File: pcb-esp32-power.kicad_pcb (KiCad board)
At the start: 2 copper layers, 52.6 x 47.4 mm, 41 parts, among them IC1 TP4054-42-SOT25-R, IC2 SY8008B, J1 C-OBD-II-16M, J2 Bus_Connector, J3 Conn_01x02, Q1 Si2307BDS, U1 STEPDOWN12_5, U2 LTC3530EMS

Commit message: OBD Pin 4 & 5 an Masse
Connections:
- J1 pad 4: Net-(J1-Pad4) -> GND

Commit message: Erste Version mit LTC4091
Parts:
- removed C2: 100nF, Capacitor_SMD:C_0603_1608Metric_Pad1.08x0.95mm_HandSolder
- removed C3: 47pF, Capacitor_SMD:C_0603_1608Metric_Pad1.08x0.95mm_HandSolder
- removed CP1: 22uF, Capacitor_Tantalum_SMD:CP_EIA-6032-28_Kemet-C_Pad2.25x2.35mm_HandSolder
- removed CP3, CP4: 10uF, Capacitor_Tantalum_SMD:CP_EIA-3528-21_Kemet-B_Pad1.50x2.35mm_HandSolder
- removed D1: B5819W, Diode_SMD:D_SOD-123
- removed IC1: TP4054-42-SOT25-R, tp4054:SOT95P280X100-5N
- removed IC2: SY8008B, SamacSys_Parts:SOT95P285X140-5N
- removed L1: 2.2uH, IP5108:CD54_Inductor
- removed Q1: Si2307BDS, Package_TO_SOT_SMD:SOT-23
- removed R10: 100k 1%, Resistor_SMD:R_0603_1608Metric_Pad0.98x0.95mm_HandSolder
- removed R6: 10K, Resistor_SMD:R_0603_1608Metric_Pad0.98x0.95mm_HandSolder
- removed R7, R8: 100k, Resistor_SMD:R_0603_1608Metric_Pad0.98x0.95mm_HandSolder
- removed R9: 453k 1%, Resistor_SMD:R_0603_1608Metric_Pad0.98x0.95mm_HandSolder
- removed U1: STEPDOWN12_5, StepDownBreakout:StepDownBreakout
- added C10: 220pF, Capacitor_SMD:C_0603_1608Metric_Pad1.08x0.95mm_HandSolder, F.Cu at (139.7, 101.9)
- added C11: 0.1uF, Capacitor_SMD:C_0603_1608Metric_Pad1.08x0.95mm_HandSolder, F.Cu at (159.5, 94.0)
- added C12: 0.47uF, Capacitor_SMD:C_0603_1608Metric_Pad1.08x0.95mm_HandSolder, F.Cu at (145.5, 95.5)
- added C13: 100uF, Capacitor_SMD:C_1210_3225Metric_Pad1.33x2.70mm_HandSolder, F.Cu at (167.4, 98.3)
- added C14: 3.3uF, Capacitor_SMD:C_0603_1608Metric_Pad1.08x0.95mm_HandSolder, F.Cu at (157.0, 94.0)
- added C15: 68uF, Capacitor_SMD:C_1206_3216Metric_Pad1.33x1.80mm_HandSolder, F.Cu at (166.9, 90.9)
- added C7: 10pF, Capacitor_SMD:C_0603_1608Metric_Pad1.08x0.95mm_HandSolder, F.Cu at (147.3, 104.1)
- added C8: 4.7uF, Capacitor_SMD:C_1206_3216Metric_Pad1.33x1.80mm_HandSolder, F.Cu at (135.1, 100.3)
- added C9: 330nF, Capacitor_SMD:C_0805_2012Metric_Pad1.18x1.45mm_HandSolder, F.Cu at (143.3, 99.1)
- added D3: 6.8V, Diode_SMD:D_SOD-123, F.Cu at (136.4, 91.4)
- added D4: B360A, Diode_SMD:D_SMA, F.Cu at (143.0, 90.7)
- added IC3: LTC4091EDJC#PBF, ltc4091:LTC4091EDJCPBF, F.Cu at (151.1, 99.3)
- added JP1: Jumper_2_Open, Jumper:SolderJumper-2_P1.3mm_Open_RoundedPad1.0x1.5mm, F.Cu at (158.0, 99.3)
- added L3: 6.8uH, ltc3530:CD54_Inductor, F.Cu at (151.1, 91.9)
- added Q2: MMDT5551, Package_TO_SOT_SMD:SOT-363_SC-70-6, F.Cu at (138.9, 99.1)
- added Q3: Si2307BDS, Package_TO_SOT_SMD:SOT-23, F.Cu at (163.1, 90.9)
- added Q4: Si2307BDS, Package_TO_SOT_SMD:SOT-23, F.Cu at (163.1, 99.1)
- added R19: 49.9k, Resistor_SMD:R_0603_1608Metric_Pad0.98x0.95mm_HandSolder, F.Cu at (140.2, 95.5)
- added R20: 100k, Resistor_SMD:R_0603_1608Metric_Pad0.98x0.95mm_HandSolder, F.Cu at (137.4, 95.5)
- added R21: 100k, Resistor_SMD:R_0603_1608Metric_Pad0.98x0.95mm_HandSolder, F.Cu at (134.9, 95.5)
- added R22: 140k, Resistor_SMD:R_0603_1608Metric_Pad0.98x0.95mm_HandSolder, F.Cu at (143.0, 95.5)
- added R23: 15k, Resistor_SMD:R_0603_1608Metric_Pad0.98x0.95mm_HandSolder, F.Cu at (143.5, 104.1)
- added R24: 105k, Resistor_SMD:R_0603_1608Metric_Pad0.98x0.95mm_HandSolder, F.Cu at (158.8, 104.1)
- added R25: 40.2k, Resistor_SMD:R_0603_1608Metric_Pad0.98x0.95mm_HandSolder, F.Cu at (143.5, 101.9)
- added R26: 10k, Resistor_SMD:R_0603_1608Metric_Pad0.98x0.95mm_HandSolder, F.Cu at (154.9, 104.1)
- added R27: 4.99k, Resistor_SMD:R_0603_1608Metric_Pad0.98x0.95mm_HandSolder, F.Cu at (163.1, 94.0)
- added R28: 0.05R, Resistor_SMD:R_0603_1608Metric_Pad0.98x0.95mm_HandSolder, F.Cu at (163.1, 96.0)
- R5: value 2K -> 10k
- moved R5 21.9 mm to (151.1, 104.1), turned to 180 degrees
- moved C4 9.69 mm to (147.1, 114.7)
- moved L2 9.69 mm to (147.8, 125.1)
- moved R14 9.69 mm to (154.7, 114.7)
- moved U2 9.69 mm to (151.6, 118.5)
- moved C6 9.69 mm to (154.4, 126.9)
- moved R15 9.69 mm to (154.4, 121.8)
- moved C1 9.69 mm to (159.8, 118.5)
- moved C5 9.69 mm to (159.8, 114.7)
- moved R11 9.69 mm to (157.2, 118.5)
- moved R12 9.69 mm to (152.1, 114.7)
- moved R13 9.69 mm to (149.6, 114.7)
- moved R16 9.69 mm to (157.2, 114.7)
- moved R17 9.69 mm to (154.4, 124.3)
- moved CP5 9.55 mm to (163.8, 116.6), turned to 90 degrees
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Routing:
- net +3V3: track 60.0 -> 32.1 mm
- net +12V: track 28.7 -> 54.7 mm
- net 5VOUT: track 44.0 -> 64.6 mm, vias 0 -> 4
- net Net-(IC3-Pad7): track 0.00 -> 18.3 mm, vias 0 -> 2
- net Net-(IC2-Pad3): track 17.8 -> 0.00 mm
- net 5VIN: track 64.4 -> 47.9 mm
- net Net-(C12-Pad1): track 0.00 -> 16.1 mm
- net Net-(C3-Pad2): track 12.5 -> 0.00 mm
- net Net-(C9-Pad1): track 0.00 -> 11.5 mm
- net Net-(C11-Pad1): track 0.00 -> 10.1 mm
- net Net-(IC3-Pad10): track 0.00 -> 10.1 mm
- net Net-(D3-Pad2): track 0.00 -> 8.91 mm
- net Net-(C7-Pad1): track 0.00 -> 8.40 mm
- net Net-(IC2-Pad1): track 7.93 -> 0.00 mm
- net Net-(IC3-Pad14): track 0.00 -> 7.88 mm
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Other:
- net class Dick: trace_width 0.4 -> 0.3
- net class Dick2 added: clearance 0.2, trace_width 0.5, via_dia 0.8, via_drill 0.4
- board text removed: "LTC3530"
- board text removed: "SY8008"

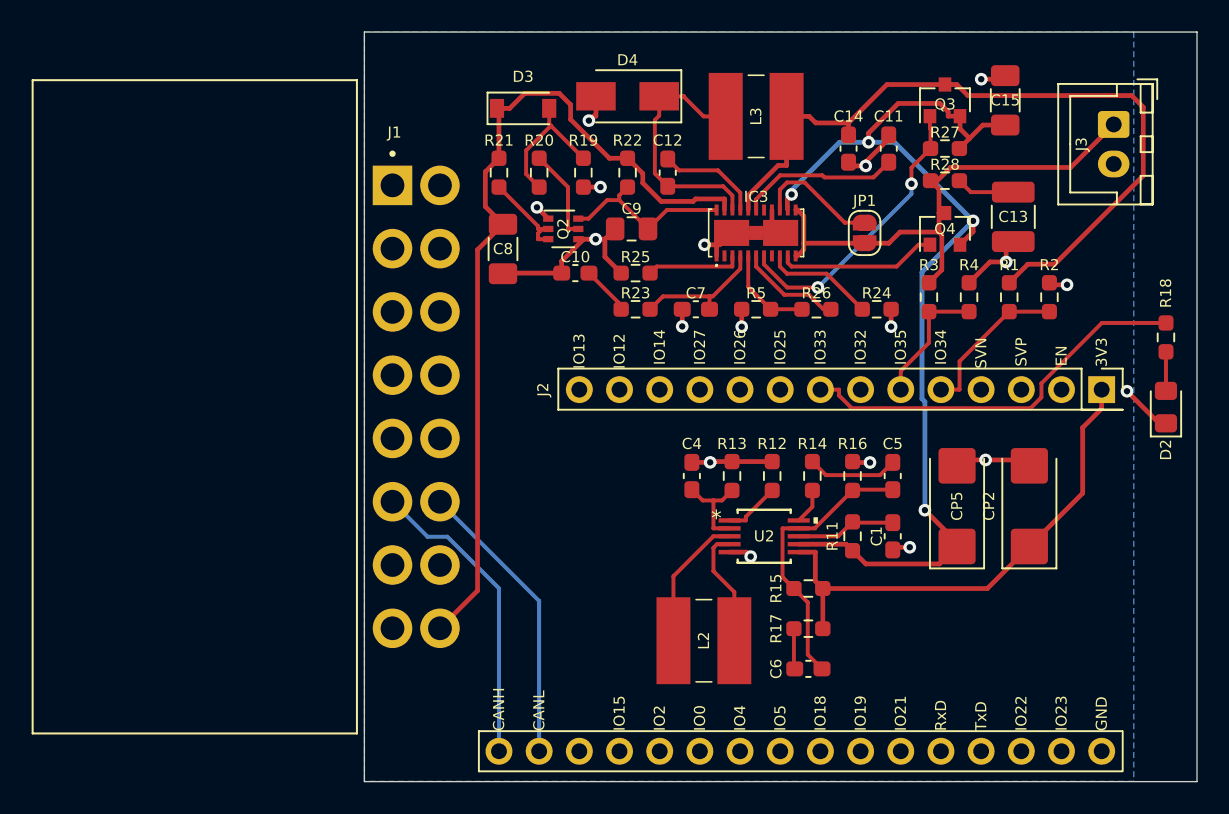
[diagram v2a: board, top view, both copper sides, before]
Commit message: Keine "Handsolder" Footprints mehr
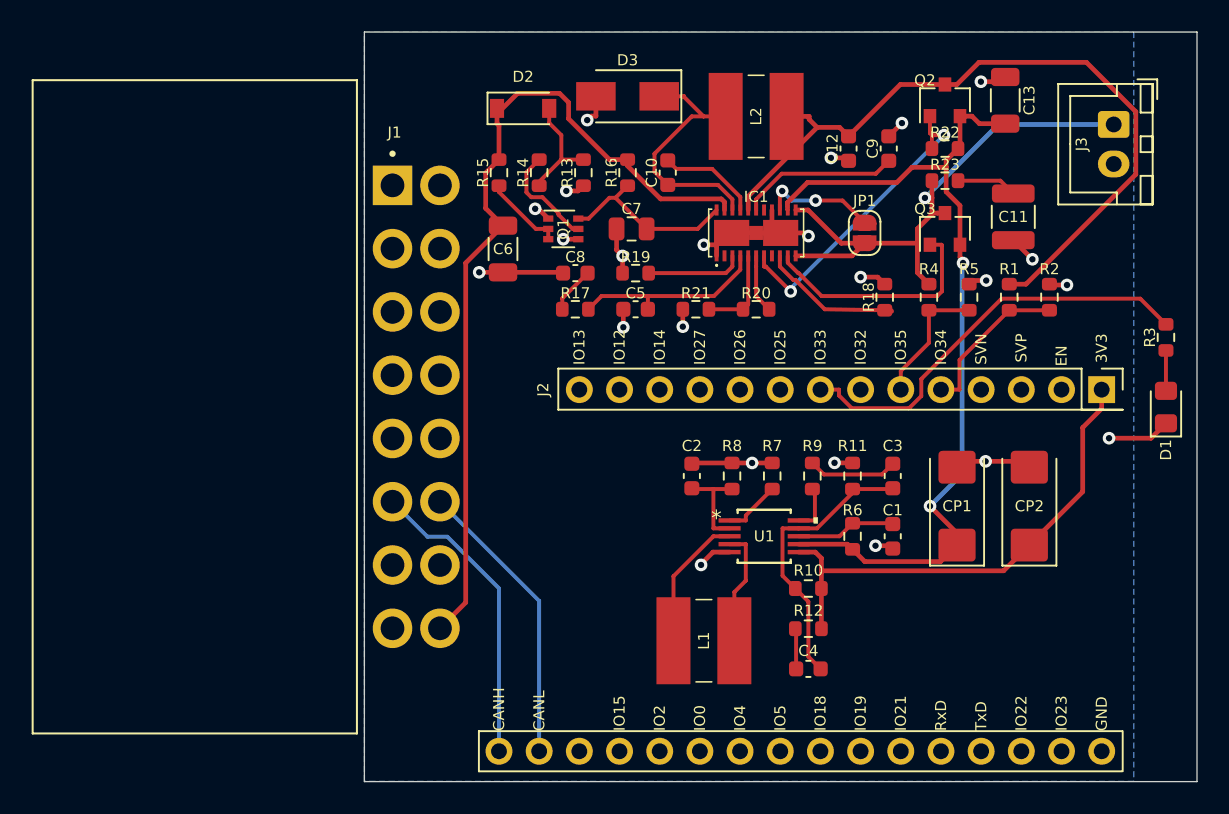
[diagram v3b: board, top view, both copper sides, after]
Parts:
- removed C14: 3.3uF, Capacitor_SMD:C_0603_1608Metric_Pad1.08x0.95mm_HandSolder
- removed C15: 68uF, Capacitor_SMD:C_1206_3216Metric_Pad1.33x1.80mm_HandSolder
- removed CP5: 22uF, Capacitor_Tantalum_SMD:CP_EIA-6032-28_Kemet-C_Pad2.25x2.35mm_HandSolder
- removed R24: 105k, Resistor_SMD:R_0603_1608Metric_Pad0.98x0.95mm_HandSolder
- removed R25: 40.2k, Resistor_SMD:R_0603_1608Metric_Pad0.98x0.95mm_HandSolder
- removed R26: 10k, Resistor_SMD:R_0603_1608Metric_Pad0.98x0.95mm_HandSolder
- removed R27: 4.99k, Resistor_SMD:R_0603_1608Metric_Pad0.98x0.95mm_HandSolder
- removed R28: 0.05R, Resistor_SMD:R_0603_1608Metric_Pad0.98x0.95mm_HandSolder
- added C2: 10nF, Capacitor_SMD:C_0603_1608Metric, F.Cu at (147.1, 114.7)
- added C3: 560pF, Capacitor_SMD:C_0603_1608Metric, F.Cu at (159.8, 114.7)
- added CP1: 22uF, Capacitor_Tantalum_SMD:CP_EIA-6032-28_Kemet-C, F.Cu at (163.8, 116.6)
- added R10: 1M, Resistor_SMD:R_0603_1608Metric, F.Cu at (154.4, 121.8)
- added R6: 1M, Resistor_SMD:R_0603_1608Metric, F.Cu at (157.2, 118.5)
- added R7: 33.2k, Resistor_SMD:R_0603_1608Metric, F.Cu at (152.1, 114.7)
- added R8: 200k, Resistor_SMD:R_0603_1608Metric, F.Cu at (149.6, 114.7)
- added R9: 10k, Resistor_SMD:R_0603_1608Metric, F.Cu at (154.7, 114.7)
- C1: footprint Capacitor_SMD:C_0603_1608Metric_Pad1.08x0.95mm_HandSolder -> Capacitor_SMD:C_0603_1608Metric
- C10: value 220pF -> 0.47uF; footprint Capacitor_SMD:C_0603_1608Metric_Pad1.08x0.95mm_HandSolder -> Capacitor_SMD:C_0603_1608Metric
- C11: value 0.1uF -> 100uF; footprint Capacitor_SMD:C_0603_1608Metric_Pad1.08x0.95mm_HandSolder -> Capacitor_SMD:C_1210_3225Metric
- C12: value 0.47uF -> 3.3uF; footprint Capacitor_SMD:C_0603_1608Metric_Pad1.08x0.95mm_HandSolder -> Capacitor_SMD:C_0603_1608Metric
- C13: value 100uF -> 68uF; footprint Capacitor_SMD:C_1210_3225Metric_Pad1.33x2.70mm_HandSolder -> Capacitor_SMD:C_1206_3216Metric
- C4: value 10nF -> 33pF; footprint Capacitor_SMD:C_0603_1608Metric_Pad1.08x0.95mm_HandSolder -> Capacitor_SMD:C_0603_1608Metric
- C5: value 560pF -> 10pF; footprint Capacitor_SMD:C_0603_1608Metric_Pad1.08x0.95mm_HandSolder -> Capacitor_SMD:C_0603_1608Metric
- C6: value 33pF -> 4.7uF; footprint Capacitor_SMD:C_0603_1608Metric_Pad1.08x0.95mm_HandSolder -> Capacitor_SMD:C_1206_3216Metric
- C7: value 10pF -> 330nF; footprint Capacitor_SMD:C_0603_1608Metric_Pad1.08x0.95mm_HandSolder -> Capacitor_SMD:C_0805_2012Metric
- C8: value 4.7uF -> 220pF; footprint Capacitor_SMD:C_1206_3216Metric_Pad1.33x1.80mm_HandSolder -> Capacitor_SMD:C_0603_1608Metric
- C9: value 330nF -> 0.1uF; footprint Capacitor_SMD:C_0805_2012Metric_Pad1.18x1.45mm_HandSolder -> Capacitor_SMD:C_0603_1608Metric
- CP2: footprint Capacitor_Tantalum_SMD:CP_EIA-6032-28_Kemet-C_Pad2.25x2.35mm_HandSolder -> Capacitor_Tantalum_SMD:CP_EIA-6032-28_Kemet-C
- R1, R17, R2, R4: footprint Resistor_SMD:R_0603_1608Metric_Pad0.98x0.95mm_HandSolder -> Resistor_SMD:R_0603_1608Metric
- R11: value 1M -> 576k; footprint Resistor_SMD:R_0603_1608Metric_Pad0.98x0.95mm_HandSolder -> Resistor_SMD:R_0603_1608Metric
- R12: value 33.2k -> 15k; footprint Resistor_SMD:R_0603_1608Metric_Pad0.98x0.95mm_HandSolder -> Resistor_SMD:R_0603_1608Metric
- R13: value 200k -> 49.9k; footprint Resistor_SMD:R_0603_1608Metric_Pad0.98x0.95mm_HandSolder -> Resistor_SMD:R_0603_1608Metric
- R14: value 10k -> 100k; footprint Resistor_SMD:R_0603_1608Metric_Pad0.98x0.95mm_HandSolder -> Resistor_SMD:R_0603_1608Metric
- R15: value 1M -> 100k; footprint Resistor_SMD:R_0603_1608Metric_Pad0.98x0.95mm_HandSolder -> Resistor_SMD:R_0603_1608Metric
- R16: value 576k -> 140k; footprint Resistor_SMD:R_0603_1608Metric_Pad0.98x0.95mm_HandSolder -> Resistor_SMD:R_0603_1608Metric
- R18: value 1K -> 105k; footprint Resistor_SMD:R_0603_1608Metric_Pad0.98x0.95mm_HandSolder -> Resistor_SMD:R_0603_1608Metric
- R19: value 49.9k -> 40.2k; footprint Resistor_SMD:R_0603_1608Metric_Pad0.98x0.95mm_HandSolder -> Resistor_SMD:R_0603_1608Metric
- R20: value 100k -> 10k; footprint Resistor_SMD:R_0603_1608Metric_Pad0.98x0.95mm_HandSolder -> Resistor_SMD:R_0603_1608Metric
- R21: value 100k -> 10k B3450; footprint Resistor_SMD:R_0603_1608Metric_Pad0.98x0.95mm_HandSolder -> Resistor_SMD:R_0603_1608Metric
- R22: value 140k -> 4.99k; footprint Resistor_SMD:R_0603_1608Metric_Pad0.98x0.95mm_HandSolder -> Resistor_SMD:R_0603_1608Metric
- R23: value 15k -> 0.05R; footprint Resistor_SMD:R_0603_1608Metric_Pad0.98x0.95mm_HandSolder -> Resistor_SMD:R_0603_1608Metric
- R3: value 470k -> 1K; footprint Resistor_SMD:R_0603_1608Metric_Pad0.98x0.95mm_HandSolder -> Resistor_SMD:R_0603_1608Metric
- R5: value 10k -> 470k; footprint Resistor_SMD:R_0603_1608Metric_Pad0.98x0.95mm_HandSolder -> Resistor_SMD:R_0603_1608Metric
- moved C6 32.8 mm to (135.1, 100.3), turned to 270 degrees
- moved R15 32.8 mm to (134.9, 95.5), turned to 270 degrees
- moved R14 25.8 mm to (137.4, 95.5)
- moved R17 25.0 mm to (139.7, 104.1)
- moved R16 23.9 mm to (143.0, 95.5), turned to 270 degrees
- moved R13 21.4 mm to (140.2, 95.5), turned to 270 degrees
- moved R23 21.2 mm to (163.1, 96.0), turned to 0 degrees
- moved R22 20.1 mm to (163.1, 94.0), turned to 0 degrees
- moved C5 19.4 mm to (143.5, 104.1), turned to 180 degrees
- moved R18 18.0 mm to (159.3, 103.4), turned to 90 degrees
- moved C9 17.0 mm to (159.5, 94.0), turned to 90 degrees
- moved R20 16.2 mm to (151.1, 104.1), turned to 180 degrees
- moved R3 15.2 mm to (177.0, 105.9)
- moved R21 15.1 mm to (147.3, 104.1), turned to 180 degrees
- moved C4 14.2 mm to (154.4, 126.9), turned to 0 degrees
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- renumbered D2 to D1, D3 to D2, D4 to D3, IC3 to IC1, L2 to L1, L3 to L2, Q2 to Q1, Q3 to Q2, Q4 to Q3, U2 to U1
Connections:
- C10 pad 2: GND -> Net-(C10-Pad2)
- C12 pad 1: Net-(C12-Pad1) -> 5VIN
- C12 pad 2: Net-(C12-Pad2) -> GND
- C13 pad 1: Net-(C13-Pad1) -> 5VOUT
- C4 pad 2: GND -> Net-(C3-Pad1)
- C5 pad 2: Net-(C5-Pad2) -> GND
- C6 pad 1: Net-(C6-Pad1) -> +12V
- C6 pad 2: Net-(C5-Pad1) -> GND
- C8 pad 1: +12V -> Net-(C8-Pad1)
- D1 pad 2: Net-(D2-Pad2) -> Net-(D1-Pad2)
- D2 pad 2: Net-(D3-Pad2) -> Net-(D2-Pad2)
- D3 pad 1: Net-(C12-Pad1) -> Net-(C10-Pad1)
- IC1 pad 17: Net-(C11-Pad1) -> Net-(C9-Pad1)
- IC1 pad 19: Net-(C12-Pad2) -> Net-(C10-Pad2)
- IC1 pad 20: Net-(C12-Pad1) -> Net-(C10-Pad1)
- IC1 pad 22: Net-(C9-Pad1) -> Net-(C7-Pad1)
- IC1 pad 3: Net-(IC3-Pad3) -> Net-(IC1-Pad3)
- IC1 pad 4: Net-(C7-Pad1) -> Net-(C5-Pad1)
- IC1 pad 5: Net-(IC3-Pad5) -> Net-(IC1-Pad5)
- IC1 pad 6: Net-(IC3-Pad6) -> Net-(IC1-Pad6)
- IC1 pad 7: Net-(IC3-Pad7) -> Net-(IC1-Pad7)
- IC1 pad 9: Net-(IC3-Pad9) -> Net-(IC1-Pad9)
- L2 pad 1: Net-(C12-Pad1) -> Net-(C10-Pad1)
- Q1 pad 2: Net-(Q2-Pad2) -> Net-(Q1-Pad2)
- Q1 pad 3: Net-(Q2-Pad2) -> Net-(Q1-Pad2)
- Q1 pad 5: Net-(Q2-Pad5) -> Net-(Q1-Pad5)
- Q1 pad 6: Net-(C9-Pad1) -> Net-(C7-Pad1)
- Q2 pad 1: Net-(IC3-Pad7) -> Net-(IC1-Pad7)
- R11 pad 1: 5VOUT -> Net-(C3-Pad1)
- R11 pad 2: Net-(C1-Pad1) -> GND
- R12 pad 1: Net-(R12-Pad1) -> +3V3
- R12 pad 2: GND -> Net-(C4-Pad1)
- R13 pad 1: Net-(C4-Pad1) -> Net-(D2-Pad2)
- R14 pad 1: Net-(C5-Pad2) -> Net-(Q1-Pad5)
- R14 pad 2: Net-(R14-Pad2) -> Net-(D2-Pad2)
- R15 pad 1: +3V3 -> +12V
- R15 pad 2: Net-(C5-Pad1) -> Net-(Q1-Pad2)
- R16 pad 1: Net-(C5-Pad1) -> +12V
- R16 pad 2: GND -> Net-(C7-Pad1)
- R17 pad 1: +3V3 -> Net-(C5-Pad1)
- R17 pad 2: Net-(C6-Pad1) -> Net-(C8-Pad1)
- R18 pad 1: LED -> Net-(IC1-Pad9)
- R18 pad 2: Net-(D2-Pad2) -> GND
- R19 pad 1: Net-(D3-Pad2) -> Net-(IC1-Pad3)
- R20 pad 1: Net-(Q2-Pad5) -> Net-(IC1-Pad6)
- R20 pad 2: Net-(D3-Pad2) -> Net-(IC1-Pad5)
- R21 pad 1: +12V -> Net-(IC1-Pad5)
- R21 pad 2: Net-(Q2-Pad2) -> GND
- R22 pad 1: +12V -> Net-(IC1-Pad7)
- R22 pad 2: Net-(C9-Pad1) -> 5VOUT
- R23 pad 1: Net-(C7-Pad1) -> +BATT
- R23 pad 2: Net-(C10-Pad1) -> Net-(C11-Pad1)
- R3 pad 1: +BATT -> LED
- R3 pad 2: BATTVOLT -> Net-(D1-Pad2)
- R4 pad 1: BATTVOLT -> +BATT
- R4 pad 2: GND -> BATTVOLT
- R5 pad 1: Net-(IC3-Pad5) -> BATTVOLT
- U1 pad 1: Net-(R12-Pad1) -> Net-(R7-Pad1)
- U1 pad 10: Net-(R14-Pad2) -> Net-(R9-Pad2)
- U1 pad 2: Net-(C4-Pad1) -> Net-(C2-Pad1)
- U1 pad 9: Net-(C5-Pad1) -> Net-(C3-Pad1)
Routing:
- net Net-(IC1-Pad7): track 0.00 -> 19.8 mm, vias 0 -> 2
- net Net-(IC3-Pad7): track 18.3 -> 0.00 mm, vias 2 -> 0
- net Net-(C3-Pad1): track 0.00 -> 18.0 mm
- net Net-(C12-Pad1): track 16.1 -> 0.00 mm
- net Net-(C10-Pad1): track 3.13 -> 16.3 mm
- net 5VOUT: track 64.6 -> 54.9 mm, vias 4 -> 2
- net Net-(D3-Pad2): track 8.91 -> 0.00 mm
- net Net-(IC1-Pad9): track 0.00 -> 8.60 mm
- net Net-(IC3-Pad9): track 7.00 -> 0.00 mm
- net Net-(Q1-Pad5): track 0.00 -> 6.69 mm
- net Net-(C12-Pad2): track 6.56 -> 0.00 mm
- net Net-(IC3-Pad6): track 6.52 -> 0.00 mm
- net Net-(C10-Pad2): track 0.00 -> 6.37 mm
- net Net-(C11-Pad1): track 10.1 -> 3.83 mm
- net Net-(IC1-Pad3): track 0.00 -> 6.14 mm
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
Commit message: Footprint Änderungen Kondensatoren & Induktoren
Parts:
- removed CP1, CP2: 22uF, Capacitor_Tantalum_SMD:CP_EIA-6032-28_Kemet-C
- added C14: 10uF, Capacitor_SMD:C_1206_3216Metric, F.Cu at (163.2, 115.5)
- added C15: 22uF, Capacitor_SMD:C_1206_3216Metric, F.Cu at (163.2, 121.8)
- C11: footprint Capacitor_SMD:C_1210_3225Metric -> Capacitor_SMD:C_1206_3216Metric
- JP1: value Jumper_2_Open -> Chrg Volt
- L1: footprint ltc3530:CD54_Inductor -> ltc3530:CKST0503
- L2: footprint ltc3530:CD54_Inductor -> ltc4091:CKST0503
- Q2, Q3: value Si2307BDS -> AO3415A
- R18: value 105k -> 200k
- moved R21 12.6 mm to (135.6, 109.0), turned to 270 degrees
- moved C4 6.86 mm to (159.8, 122.6), turned to 90 degrees
- moved C5 3.81 mm to (147.3, 104.1)
- moved R17 3.81 mm to (143.5, 104.1)
- moved R12 3.31 mm to (157.2, 122.6), turned to 270 degrees
- moved L1 1.59 mm to (149.2, 124.3), turned to 180 degrees
- moved R10 0.80 mm to (154.7, 122.6), turned to 270 degrees
- moved C13 0.68 mm to (167.1, 91.6)
- moved C11 0.25 mm to (167.1, 98.3)
- turned L2 to 0 degrees
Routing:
- net Net-(IC1-Pad5): track 5.67 -> 19.8 mm
- net Net-(C5-Pad1): track 12.4 -> 8.64 mm
- net +3V3: track 31.6 -> 28.3 mm
- net Net-(C3-Pad1): track 18.0 -> 20.0 mm
- net Net-(L1-Pad2): track 8.67 -> 7.58 mm
- net Net-(L1-Pad1): track 7.43 -> 6.68 mm
- net GND: track 51.8 -> 51.1 mm, vias 23 -> 24

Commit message: Nochmal überarbeitet
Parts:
- R22: value 4.99k -> 10k
- moved C2 10.7 mm to (151.4, 124.5), turned to 270 degrees
- moved L1 6.87 mm to (156.0, 122.9)
- moved C14 6.73 mm to (169.7, 117.3)
- moved C15 6.68 mm to (169.7, 123.4)
- moved C1 6.63 mm to (166.1, 120.4)
- moved C4 6.63 mm to (166.1, 124.5)
- moved R6 6.63 mm to (163.6, 120.4)
- moved R10 6.63 mm to (161.0, 124.5)
- moved R12 6.63 mm to (163.6, 124.5)
- moved C3 6.56 mm to (166.1, 116.3)
- moved R11 6.56 mm to (163.6, 116.3)
- moved R9 6.56 mm to (161.0, 116.3)
- moved R8 5.99 mm to (151.4, 120.4)
- moved U1 4.77 mm to (156.0, 116.5)
- moved R5 2.55 mm to (162.1, 103.6)
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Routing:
- net Net-(C3-Pad1): track 20.0 -> 33.5 mm
- net 5VIN: track 47.8 -> 37.9 mm
- net +BATT: track 35.6 -> 45.5 mm, vias 1 -> 0
- net 5VOUT: track 55.0 -> 63.2 mm, vias 2 -> 3
- net GND: track 51.1 -> 44.2 mm, vias 24 -> 22
- net Net-(IC1-Pad10): track 14.9 -> 9.90 mm
- net Net-(C2-Pad1): track 6.07 -> 10.8 mm
- net Net-(C1-Pad1): track 6.31 -> 9.34 mm
- net Net-(D2-Pad2): track 7.18 -> 10.1 mm
- net Net-(C9-Pad1): track 10.1 -> 7.44 mm
- net Net-(IC1-Pad9): track 8.60 -> 6.01 mm
- net +3V3: track 28.3 -> 30.8 mm
- net Net-(Q1-Pad5): track 6.69 -> 8.93 mm
- net +12V: track 54.5 -> 56.7 mm
- net EXTPOW: track 10.0 -> 8.04 mm
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
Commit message: Massefläche + Kleinigkeiten
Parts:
- moved C12 2.09 mm to (157.7, 91.9), turned to 0 degrees
- moved C9 2.09 mm to (157.7, 94.0)
- moved J3 2.03 mm to (173.7, 94.5)
- moved C7 0.57 mm to (143.3, 98.8)
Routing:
- net Net-(Q1-Pad5): track 8.93 -> 5.53 mm
- net +BATT: track 45.5 -> 43.3 mm
- net 5VIN: track 37.9 -> 36.9 mm
- net GND: track 44.2 -> 45.1 mm, vias 22 -> 30
- net Net-(IC1-Pad3): track 6.29 -> 7.06 mm
- added copper zone on F.Cu, net GND
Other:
- net class Dick2: trace_width 0.5 -> 0.4
